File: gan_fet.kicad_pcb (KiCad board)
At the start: 2 copper layers, 13 x 22.2 mm, 6 parts, among them J1 Conn_01x04_Male, Q1 EPC2036, U1 NPC81074

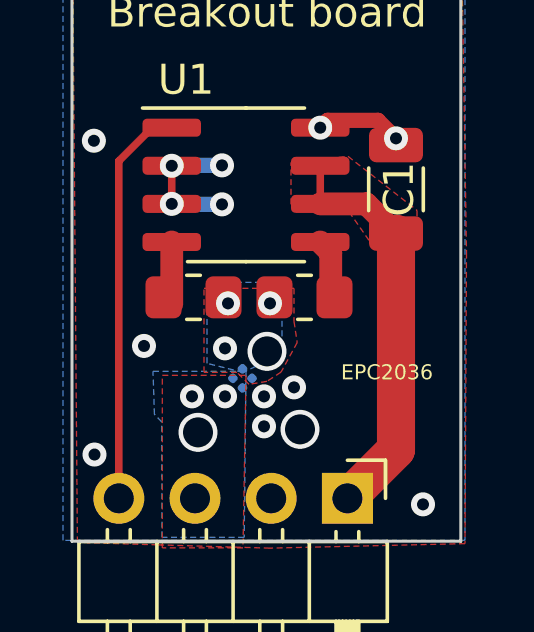
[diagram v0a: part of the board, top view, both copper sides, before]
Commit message: Fixed mosfet symbol and pinout
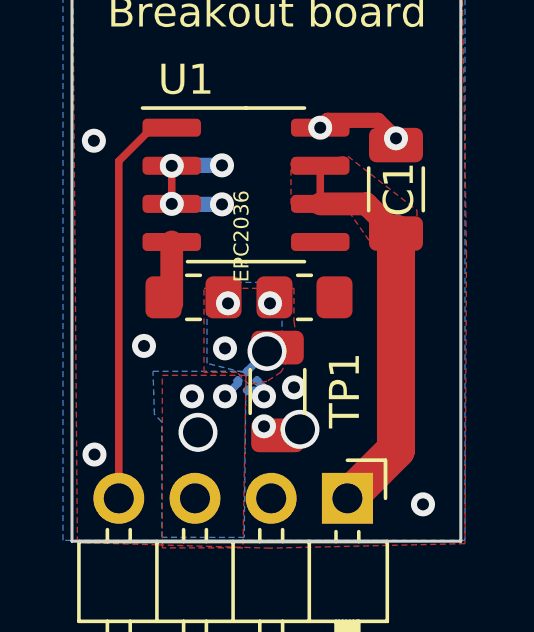
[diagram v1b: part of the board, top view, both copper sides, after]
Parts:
- added TP1: C_Small, Resistor_SMD:R_1206_3216Metric, F.Cu at (143.8, 95.5)
- moved Q1 0.73 mm to (142.8, 94.5), turned to -135 degrees
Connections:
- Q1 pad 1: GND -> /fetGate
- Q1 pad 2: /drain -> GND
- Q1 pad 3: /fetGate -> /drain
- Q1 pad 4: /drain -> GND
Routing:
- net Net-(R2-Pad1): track 2.24 -> 0.00 mm
- net GND: track 7.51 -> 8.75 mm
- net /fetGate: track 0.00 -> 0.93 mm
- net /drain: track 0.00 -> 0.70 mm
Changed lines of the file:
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@@
+    )
+  )
+  (footprint "Resistor_SMD:R_1206_3216Metric" (layer "F.Cu")
+    (at 143.75 95.5375 -90)
+    (descr "Resistor SMD 1206 (3216 Metric), square (rectangular) end terminal, IPC_7351 nominal, (Body size source: IPC-SM-782 page 72, https://www.pcb-3d.com/wordpress/wp-content/uploads/ipc-sm-782a_amendment_1_and_2.pdf), generated with kicad-footprint-generator")
+    (tags "resistor")
+    (property "Sheetfile" "gan_fet.kicad_sch")
+    (property "Sheetname" "")
+    (attr smd)
+    (fp_text reference "TP1" (at -0.0375 -2.25 90) (layer "F.SilkS")
+      (effects (font (size 1 1) (thickness 0.15)))
+    )
+    (fp_text value "C_Small" (at 0 1.82 90) (layer "F.Fab")
+      (effects (font (size 1 1) (thickness 0.15)))
+    )
+    (fp_text user "${REFERENCE}" (at 0 0 90) (layer "F.Fab")
+      (effects (font (size 0.8 0.8) (thickness 0.12)))
+    )
+    (fp_line (start -0.727064 -0.91) (end 0.727064 -0.91) (layer "F.SilkS") (width 0.12))
+    (fp_line (start -0.727064 0.91) (end 0.727064 0.91) (layer "F.SilkS") (width 0.12))
+    (fp_line (start 2.28 1.12) (end -2.28 1.12) (layer "F.CrtYd") (width 0.05))
+    (fp_line (start -2.28 -1.12) (end 2.28 -1.12) (layer "F.CrtYd") (width 0.05))
+    (fp_line (start 2.28 -1.12) (end 2.28 1.12) (layer "F.CrtYd") (width 0.05))
+    (fp_line (start -2.28 1.12) (end -2.28 -1.12) (layer "F.CrtYd") (width 0.05))
+    (fp_line (start -1.6 -0.8) (end 1.6 -0.8) (layer "F.Fab") (width 0.1))
+    (fp_line (start 1.6 -0.8) (end 1.6 0.8) (layer "F.Fab") (width 0.1))
+    (fp_line (start -1.6 0.8) (end -1.6 -0.8) (layer "F.Fab") (width 0.1))
+    (fp_line (start 1.6 0.8) (end -1.6 0.8) (layer "F.Fab") (width 0.1))
+    (pad "1" smd roundrect (at -1.4625 0 270) (size 1.125 1.75) (layers "F.Cu" "F.Paste" "F.Mask") (roundrect_rratio 0.222222)
+      (net 7 "/fetGate") (pintype "passive"))
+    (pad "2" smd roundrect (at 1.4625 0 270) (size 1.125 1.75) (layers "F.Cu" "F.Paste" "F.Mask") (roundrect_rratio 0.222222)
+      (net 2 "GND") (pintype "passive"))
+    (model "${KICAD6_3DMODEL_DIR}/Resistor_SMD.3dshapes/R_1206_3216Metric.wrl"
+      (offset (xyz 0 0 0))
+      (scale (xyz 1 1 1))
+      (rotate (xyz 0 0 0))
     )
   )
@@
   )
   (footprint "epc:epc2036" (layer "B.Cu")
-    (at 143.218198 95.1 135)
+    (at 142.75 94.545406 -135)
     (property "Sheetfile" "gan_fet.kicad_sch")
     (property "Sheetname" "")
     (attr smd)
-    (fp_text reference "Q1" (at -0.544472 -1.435427 45 unlocked) (layer "B.SilkS")
+    (fp_text reference "Q1" (at -0.544472 -1.435427 -225 unlocked) (layer "B.SilkS")
       (effects (font (size 0.5 0.5) (thickness 0.1)) (justify mirror))
     )
-    (fp_text value "EPC2036" (at -2.815559 3.098402 unlocked) (layer "F.SilkS")
+    (fp_text value "EPC2036" (at -2.815559 3.098402 -270 unlocked) (layer "F.SilkS")
       (effects (font (size 0.5 0.5) (thickness 0.1)))
     )
-    (fp_text user "${REFERENCE}" (at 0.95 -1.905 45 unlocked) (layer "B.Fab")
+    (fp_text user "${REFERENCE}" (at 0.95 -1.905 -225 unlocked) (layer "B.Fab")
       (effects (font (size 0.5 0.5) (thickness 0.1)) (justify mirror))
     )
@@
     (fp_circle (center 0.225 -0.225) (end 0.325 -0.225) (layer "B.Mask") (width 0) (fill solid))
     (fp_rect (start 0.95 0.05) (end -0.05 -0.95) (layer "B.Fab") (width 0.1) (fill none))
-    (pad "1" smd roundrect (at 0.225 -0.225 135) (size 0.287 0.287) (property pad_prop_bga) (layers "B.Cu" "B.Paste") (roundrect_rratio 0.3333344948)
+    (pad "1" smd roundrect (at 0.225 -0.225 225) (size 0.287 0.287) (property pad_prop_bga) (layers "B.Cu" "B.Paste") (roundrect_rratio 0.3333344948)
+      (net 7 "/fetGate") (pinfunction "G") (pintype "input") (solder_mask_margin -0.05) (solder_paste_margin -0.025) (zone_connect 2))
+    (pad "2" smd roundrect (at 0.225 -0.675 225) (size 0.287 0.287) (property pad_prop_bga) (layers "B.Cu" "B.Paste") (roundrect_rratio 0.3333344948)
       (net 2 "GND") (pinfunction "S") (pintype "passive") (solder_mask_margin -0.05) (solder_paste_margin -0.025) (zone_connect 2))
-    (pad "2" smd roundrect (at 0.225 -0.675 135) (size 0.287 0.287) (property pad_prop_bga) (layers "B.Cu" "B.Paste") (roundrect_rratio 0.3333344948)
+    (pad "3" smd roundrect (at 0.675 -0.225 225) (size 0.287 0.287) (property pad_prop_bga) (layers "B.Cu" "B.Paste") (roundrect_rratio 0.3333344948)
       (net 4 "/drain") (pinfunction "D") (pintype "passive") (solder_mask_margin -0.05) (solder_paste_margin -0.025) (zone_connect 2))
-    (pad "3" smd roundrect (at 0.675 -0.225 135) (size 0.287 0.287) (property pad_prop_bga) (layers "B.Cu" "B.Paste") (roundrect_rratio 0.3333344948)
-      (net 7 "/fetGate") (pinfunction "G") (pintype "input") (solder_mask_margin -0.05) (solder_paste_margin -0.025) (zone_connect 2))
-    (pad "4" smd roundrect (at 0.675 -0.675 135) (size 0.287 0.287) (property pad_prop_bga) (layers "B.Cu" "B.Paste") (roundrect_rratio 0.3333344948)
-      (net 4 "/drain") (pinfunction "D") (pintype "passive") (solder_mask_margin -0.05) (solder_paste_margin -0.025) (zone_connect 2))
+    (pad "4" smd roundrect (at 0.675 -0.675 225) (size 0.287 0.287) (property pad_prop_bga) (layers "B.Cu" "B.Paste") (roundrect_rratio 0.3333344948)
+      (net 2 "GND") (pinfunction "D") (pintype "passive") (solder_mask_margin -0.05) (solder_paste_margin -0.025) (zone_connect 2))
     (model "/home/frosty/Downloads/D0353.step"
       (offset (xyz 5 4.575 0))
@@
   (via (at 145.175 86.745) (size 0.8) (drill 0.4) (layers "F.Cu" "B.Cu") (net 2))
   (via (at 139.3 94.02) (size 0.8) (drill 0.4) (layers "F.Cu" "B.Cu") (free) (net 2))
+  (segment (start 143.1 95.5) (end 143.3 95.7) (width 0.254) (layer "B.Cu") (net 2))
   (segment (start 140.24 89.3) (end 140.225 89.285) (width 0.254) (layer "B.Cu") (net 2))
   (segment (start 141.9 88) (end 140.24 88) (width 0.508) (layer "B.Cu") (net 2))
   (segment (start 140.24 88) (end 140.225 88.015) (width 0.254) (layer "B.Cu") (net 2))
+  (segment (start 142.75 95.5) (end 143.1 95.5) (width 0.254) (layer "B.Cu") (net 2))
   (segment (start 141.9 89.3) (end 140.24 89.3) (width 0.508) (layer "B.Cu") (net 2))
+  (segment (start 143.068198 95.181802) (end 143.3 95.413604) (width 0.254) (layer "B.Cu") (net 2))
+  (segment (start 143.3 95.413604) (end 143.3 95.7) (width 0.254) (layer "B.Cu") (net 2))
   (segment (start 138.46 99.1) (end 138.46 87.85798) (width 0.254) (layer "F.Cu") (net 3))
   (segment (start 138.46 87.85798) (end 139.57298 86.745) (width 0.254) (layer "F.Cu") (net 3))
@@
   (via (at 141.1 96.9) (size 1.3) (drill 1) (layers "F.Cu" "B.Cu") (free) (net 4))
   (via (at 140.9 95.7) (size 0.8) (drill 0.4) (layers "F.Cu" "B.Cu") (free) (net 4))
+  (segment (start 142.431802 95.181802) (end 142.431802 95.268198) (width 0.254) (layer "B.Cu") (net 4))
+  (segment (start 142.431802 95.268198) (end 142 95.7) (width 0.254) (layer "B.Cu") (net 4))
   (segment (start 140.225 90.555) (end 140.225 92.625) (width 0.762) (layer "F.Cu") (net 5))
-  (segment (start 145.175 90.555) (end 145.525 90.905) (width 0.762) (layer "F.Cu") (net 6))
-  (segment (start 145.525 90.905) (end 145.525 92.65) (width 0.762) (layer "F.Cu") (net 6))
   (via (at 142 94.1) (size 0.8) (drill 0.4) (layers "F.Cu" "B.Cu") (free) (net 7))
   (via (at 143.4 94.2) (size 1.3) (drill 1) (layers "F.Cu" "B.Cu") (net 7))
   (via (at 143.5 92.6) (size 0.8) (drill 0.4) (layers "F.Cu" "B.Cu") (net 7))
   (via (at 142.1 92.6) (size 0.8) (drill 0.4) (layers "F.Cu" "B.Cu") (net 7))
+  (segment (start 142.75 94.863604) (end 142.75 94.85) (width 0.254) (layer "B.Cu") (net 7))
+  (segment (start 142.75 94.85) (end 143.4 94.2) (width 0.254) (layer "B.Cu") (net 7))
   (zone (net 2) (net_name "GND") (layer "F.Cu") (hatch edge 0.508)
     (connect_pads yes (clearance 0.1524))

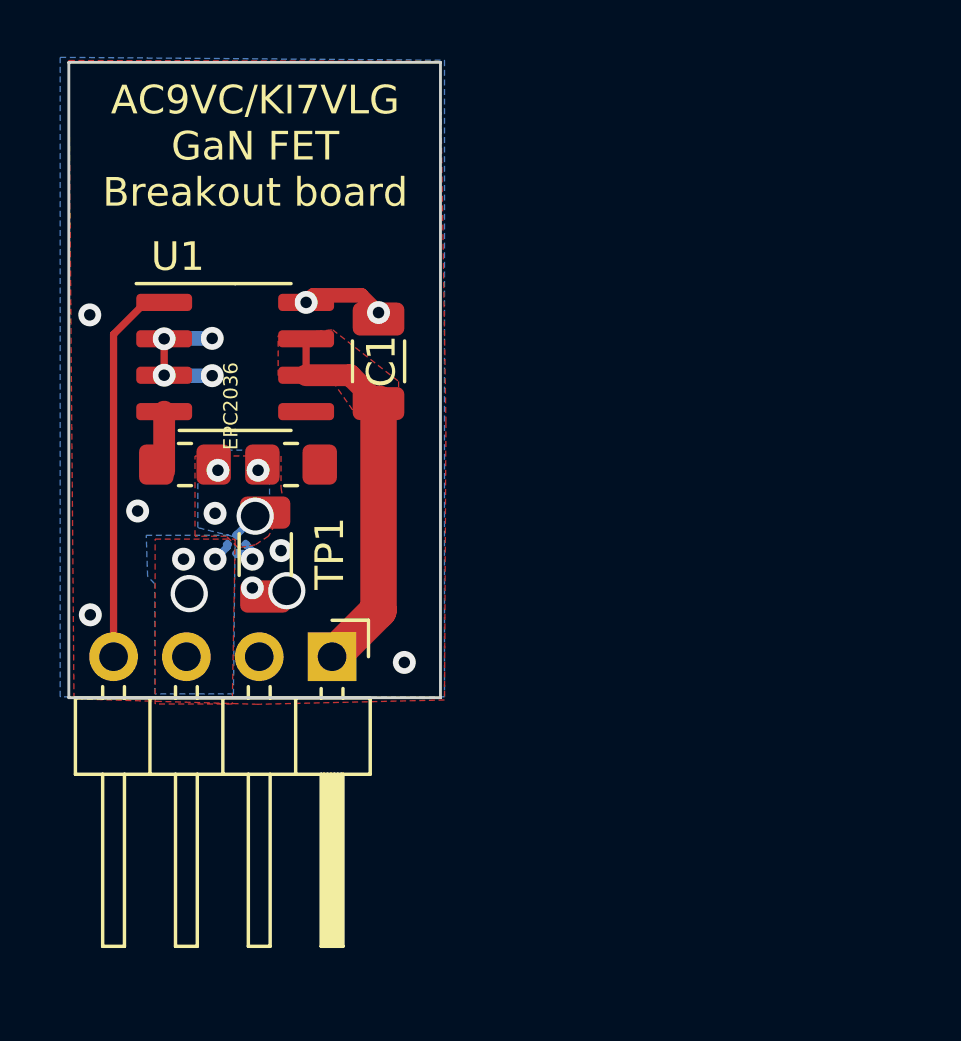
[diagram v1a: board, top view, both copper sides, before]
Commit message: Downsized board and replaced driver
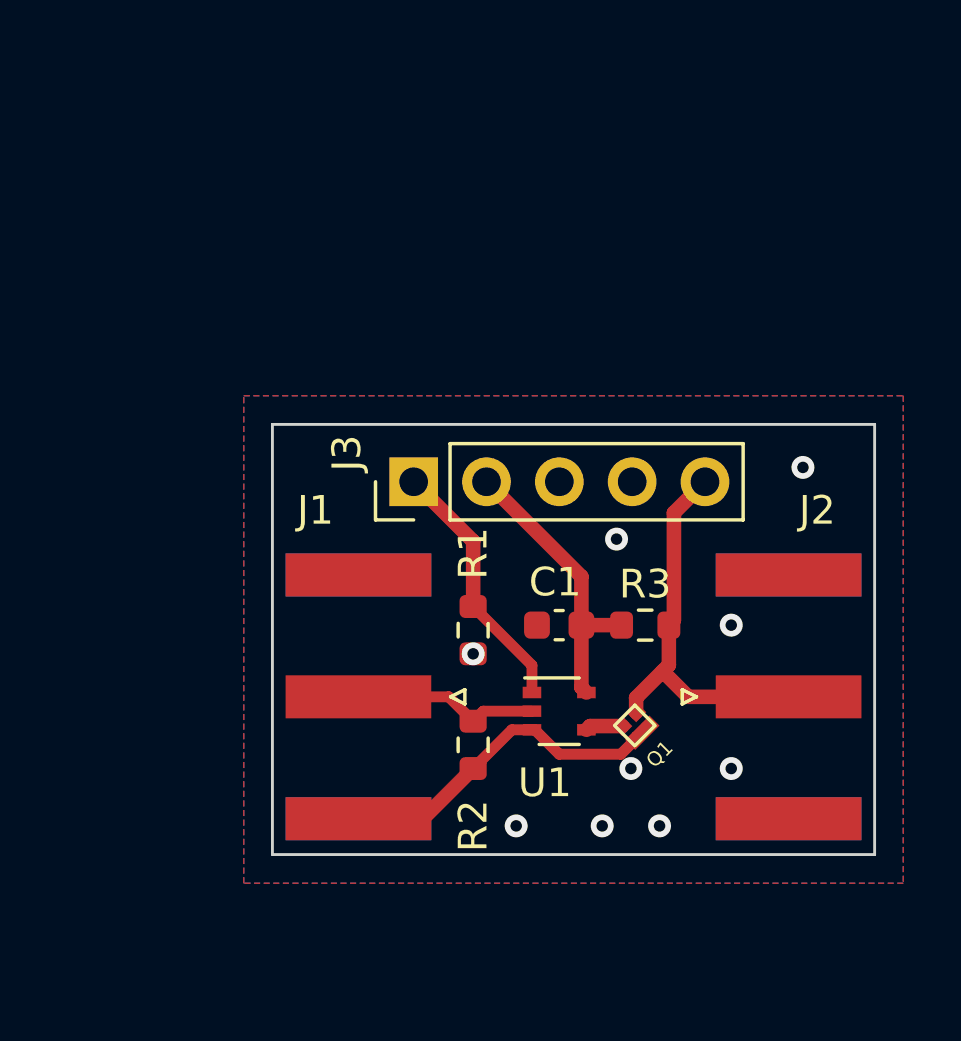
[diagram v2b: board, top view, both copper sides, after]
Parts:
- removed TP1: C_Small, Resistor_SMD:R_1206_3216Metric
- added J2: Conn_Coaxial, Connector_Coaxial:SMA_Amphenol_132289_EdgeMount, F.Cu at (162.0, 100.5)
- added J3: Conn_01x05_Male, Connector_PinHeader_2.54mm:PinHeader_1x05_P2.54mm_Vertical, F.Cu at (148.9, 93.0)
- added R3: 50, Resistor_SMD:R_0603_1608Metric, F.Cu at (157.0, 98.0)
- C1: value 100n -> 1n; footprint Capacitor_SMD:C_1206_3216Metric -> Capacitor_SMD:C_0603_1608Metric
- J1: value Conn_01x04_Male -> Conn_Coaxial; footprint Connector_PinHeader_2.54mm:PinHeader_1x04_P2.54mm_Horizontal -> Connector_Coaxial:SMA_Amphenol_132289_EdgeMount
- Q1: value EPC2036 -> EPC2038; moved to F.Cu
- R1: value 1 -> 1k; footprint Resistor_SMD:R_0805_2012Metric_Pad1.20x1.40mm_HandSolder -> Resistor_SMD:R_0603_1608Metric
- R2: value 4.7 -> 1k; footprint Resistor_SMD:R_0805_2012Metric_Pad1.20x1.40mm_HandSolder -> Resistor_SMD:R_0603_1608Metric
- U1: value NPC81074 -> 74LVC1G32SE-7; footprint Package_SO:SOIC-8_3.9x4.9mm_P1.27mm -> Package_TO_SOT_SMD:SOT-353_SC-70-5
- moved U1 16.7 mm to (154.0, 101.0)
- moved Q1 15.0 mm to (156.0, 101.5), turned to 45 degrees
- moved R2 11.7 mm to (151.0, 102.2), turned to -90 degrees
- moved R1 11.6 mm to (151.0, 98.2), turned to -90 degrees
- moved C1 11.2 mm to (154.0, 98.0), turned to 180 degrees
- moved J1 1.68 mm to (147.0, 100.5), turned to 180 degrees
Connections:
- J1 pad 1: +5V -> /B
- Q1 pad 1: /fetGate -> /Gate
- Q1 pad 3: /drain -> /Drain
- R1 pad 1: Net-(R1-Pad1) -> /A
- R1 pad 2: /fetGate -> GND
- R2 pad 1: Net-(R2-Pad1) -> /B
- R2 pad 2: /fetGate -> GND
- U1 pad 1: /gate -> /A
- U1 pad 2: GND -> /B
- U1 pad 4: Net-(R1-Pad1) -> /Gate
- U1 pad 5: Net-(R2-Pad1) -> +5V
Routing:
- net /Drain: track 0.00 -> 13.8 mm
- net /gate: track 12.8 -> 0.00 mm
- net /A: track 0.00 -> 9.06 mm
- net /B: track 0.00 -> 6.55 mm
- net +5V: track 14.0 -> 10.2 mm
- net GND: track 8.75 -> 11.8 mm, vias 14 -> 9
- net Net-(R1-Pad1): track 2.07 -> 0.00 mm
- net /Gate: track 0.00 -> 1.30 mm
- net /fetGate: track 0.93 -> 0.00 mm, vias 4 -> 0
- net /drain: track 0.70 -> 0.00 mm, vias 3 -> 0
- removed copper zone on F.Cu, net +5V
- removed copper zone on B.Cu, net /drain
- removed copper zone on F.Cu, net /drain
- removed copper zone on B.Cu, net /fetGate
- removed copper zone on F.Cu, net /fetGate
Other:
- board size 13 x 22.2 mm -> 21 x 15 mm
- board text removed: "+5 S D G"
- board text removed: "AC9VC/KI7VLG GaN FET Breakout board"

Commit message: Downsized to reduce gate inductance
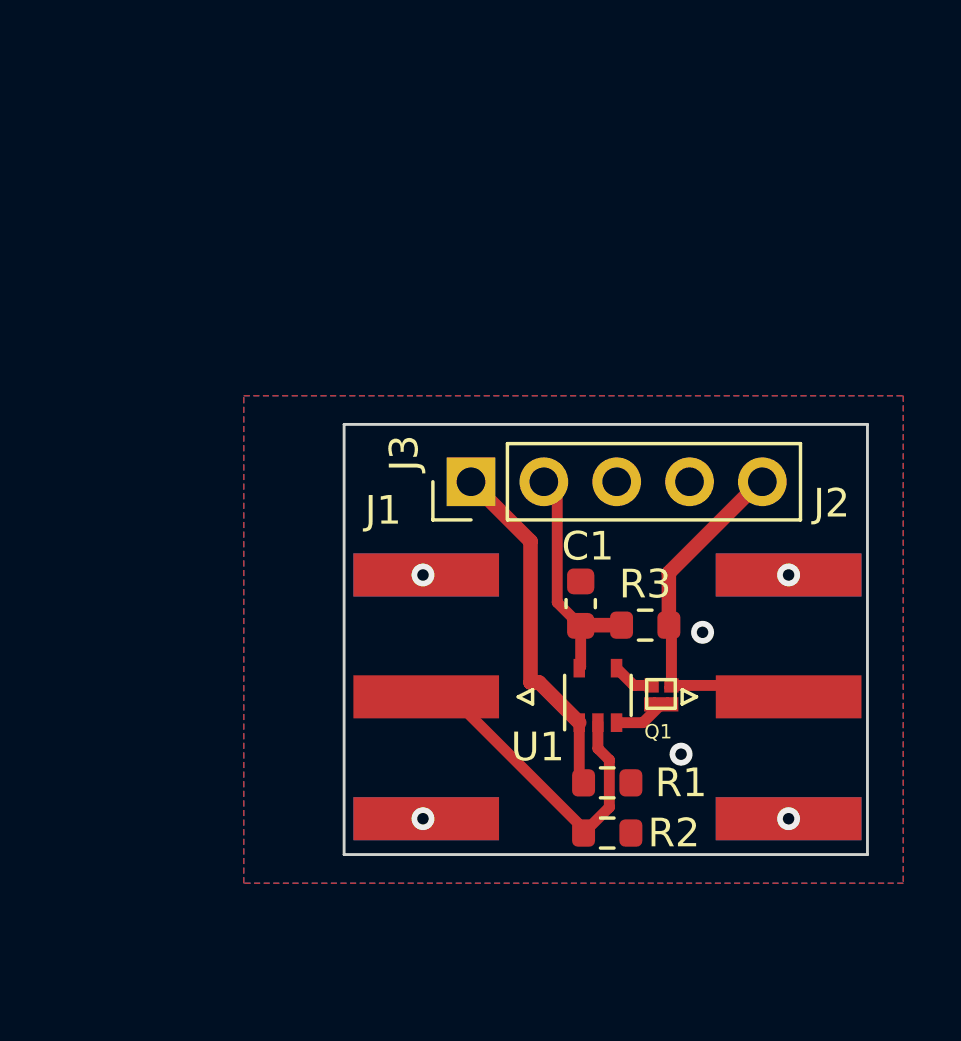
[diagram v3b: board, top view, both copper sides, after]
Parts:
- moved R1 7.09 mm to (155.7, 103.5), turned to 0 degrees
- moved R2 5.60 mm to (155.7, 105.2), turned to 0 degrees
- moved J1 2.36 mm to (149.4, 100.5)
- moved J3 2.00 mm to (150.9, 93.0)
- moved Q1 1.90 mm to (157.1, 100.0), turned to 0 degrees
- moved U1 1.46 mm to (155.3, 100.5), turned to 90 degrees
- moved C1 1.06 mm to (154.8, 97.2), turned to 90 degrees
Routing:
- net GND: track 11.8 -> 1.82 mm, vias 9 -> 6
- net /B: track 6.55 -> 11.9 mm
- net /A: track 9.06 -> 12.3 mm
- net +5V: track 10.2 -> 8.45 mm
- net /Drain: track 13.8 -> 12.8 mm
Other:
- board size 21 x 15 mm -> 18.2 x 15 mm
- board text added: "D GND +5 A"
- board text added: "gan_fet mini test board August 18 2022"

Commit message: Added header for standard filter board
Moved R3 to tie to 12V instead of 5V
Swapped inputs on OR gate
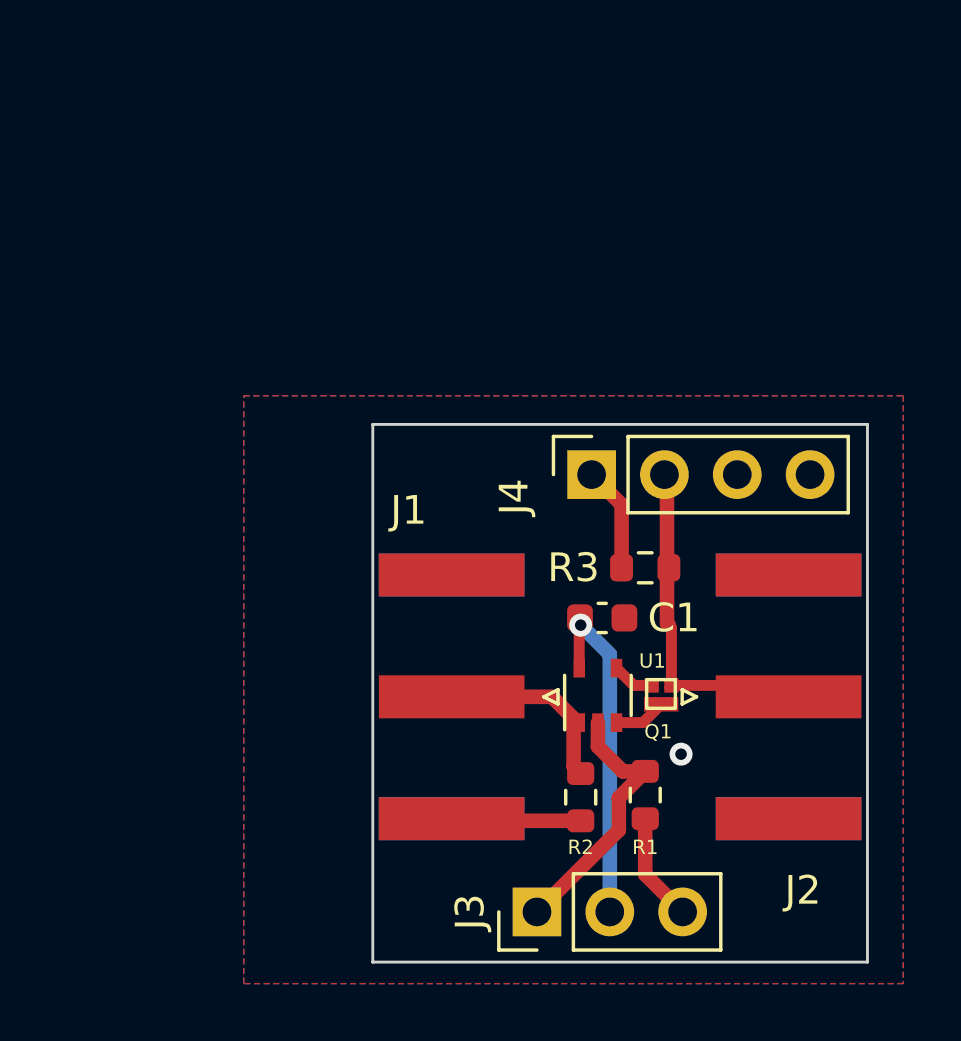
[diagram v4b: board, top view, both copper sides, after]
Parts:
- added J4: Conn_01x04_Female, Connector_PinSocket_2.54mm:PinSocket_1x04_P2.54mm_Vertical, F.Cu at (155.1, 92.8)
- J3: value Conn_01x05_Male -> Conn_01x03_Male; footprint Connector_PinHeader_2.54mm:PinHeader_1x05_P2.54mm_Vertical -> Connector_PinHeader_2.54mm:PinHeader_1x03_P2.54mm_Vertical
- moved J3 15.2 mm to (153.2, 108.0)
- moved R3 2.00 mm to (157.0, 96.0)
- moved R2 1.56 mm to (154.8, 104.0), turned to -90 degrees
- moved R1 1.39 mm to (157.0, 103.9), turned to -90 degrees
- moved C1 0.90 mm to (155.5, 97.8), turned to 0 degrees
- moved J1 0.89 mm to (150.2, 100.5)
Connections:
- J1 pad 1: /B -> /A
- J2 pad 1: /Drain -> /Tx
- J3 pad 1: /A -> /B
- Q1 pad 3: /Drain -> /Tx
- R1 pad 1: /A -> /B
- R2 pad 1: /B -> /A
- R3 pad 1: +5V -> +12V
- R3 pad 2: /Drain -> /Tx
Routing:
- net /Drain: track 12.8 -> 0.00 mm
- net /Tx: track 0.00 -> 11.6 mm
- net GND: track 1.82 -> 9.64 mm, vias 6 -> 1
- net /A: track 12.3 -> 6.09 mm
- net +12V: track 0.00 -> 3.68 mm
- net +5V: track 8.45 -> 12.0 mm, vias 0 -> 1
- net /B: track 11.9 -> 9.31 mm
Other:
- board size 18.2 x 15 mm -> 17.2 x 18.8 mm
- board text added: "GND +5 B"
- board text added: "GND Rx Tx 12"
- board text added: "gan fet mini test board August 18 2022"
- board text removed: "D GND +5 A"
- board text removed: "gan_fet mini test board August 18 2022"
